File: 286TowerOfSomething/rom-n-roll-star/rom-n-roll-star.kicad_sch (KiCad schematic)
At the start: 15 parts, among them J1 Bus_ISA_8bit, SW1 SW_DIP_x08, U1 SST39SF010, U2 74ALS688

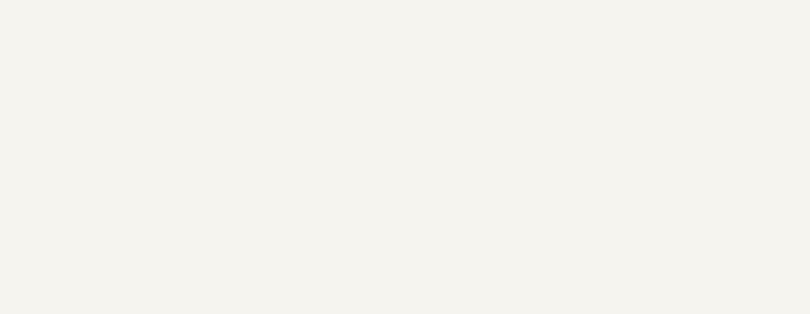
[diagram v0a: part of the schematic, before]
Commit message: Adding ISA bracked to rom-n-roll-star
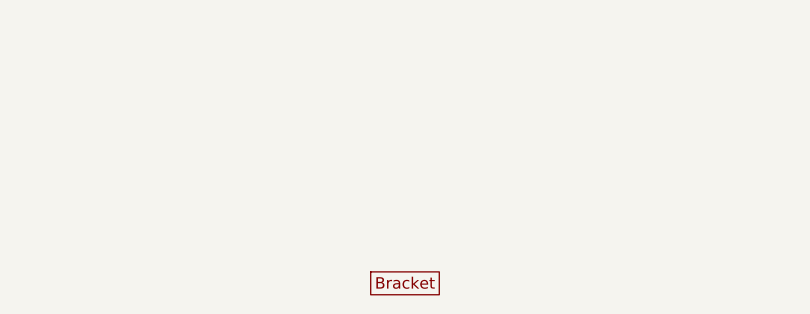
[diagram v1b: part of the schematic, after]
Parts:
- added BRACKET1: ~, pc-parts:PC_BRACKET_ISA_KEYSTONE_9202_Rev1, symbol pc-parts:9202
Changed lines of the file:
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@@
+	)
+	(symbol
+		(lib_id "pc-parts:9202")
+		(at 139.7 190.5 0)
+		(unit 1)
+		(exclude_from_sim no)
+		(in_bom yes)
+		(on_board yes)
+		(dnp no)
+		(fields_autoplaced yes)
+		(property "Reference" "BRACKET1"
+			(at 139.7 190.5 0)
+			(effects
+				(font
+					(size 1.27 1.27)
+				)
+				(hide yes)
+			)
+		)
+		(property "Value" "~"
+			(at 144.78 190.5 0)
+			(effects
+				(font
+					(size 1.27 1.27)
+				)
+				(justify left)
+			)
+		)
+		(property "Footprint" "pc-parts:PC_BRACKET_ISA_KEYSTONE_9202_Rev1"
+			(at 139.7 190.5 0)
+			(effects
+				(font
+					(size 1.27 1.27)
+				)
+				(hide yes)
+			)
+		)
+		(property "Datasheet" ""
+			(at 139.7 190.5 0)
+			(effects
+				(font
+					(size 1.27 1.27)
+				)
+				(hide yes)
+			)
+		)
+		(property "Description" ""
+			(at 139.7 190.5 0)
+			(effects
+				(font
+					(size 1.27 1.27)
+				)
+				(hide yes)
+			)
+		)
+		(instances
+			(project ""
+				(path "/29e749aa-55d9-42fb-8318-49af17b07430"
+					(reference "BRACKET1")
+					(unit 1)
+				)
+			)
+		)
 	)
 	(symbol
